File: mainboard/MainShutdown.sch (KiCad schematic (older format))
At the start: 28 parts, among them K2 G6DN 12V, Q2 DMN10H220L, Q8 NTR5105PT1G, Q9 NTR5105PT1G, SW2 SD_RESET, U13 TS3704IPT, U14 CD4044, U15 CD4082, U4 MainBoard_AD8244

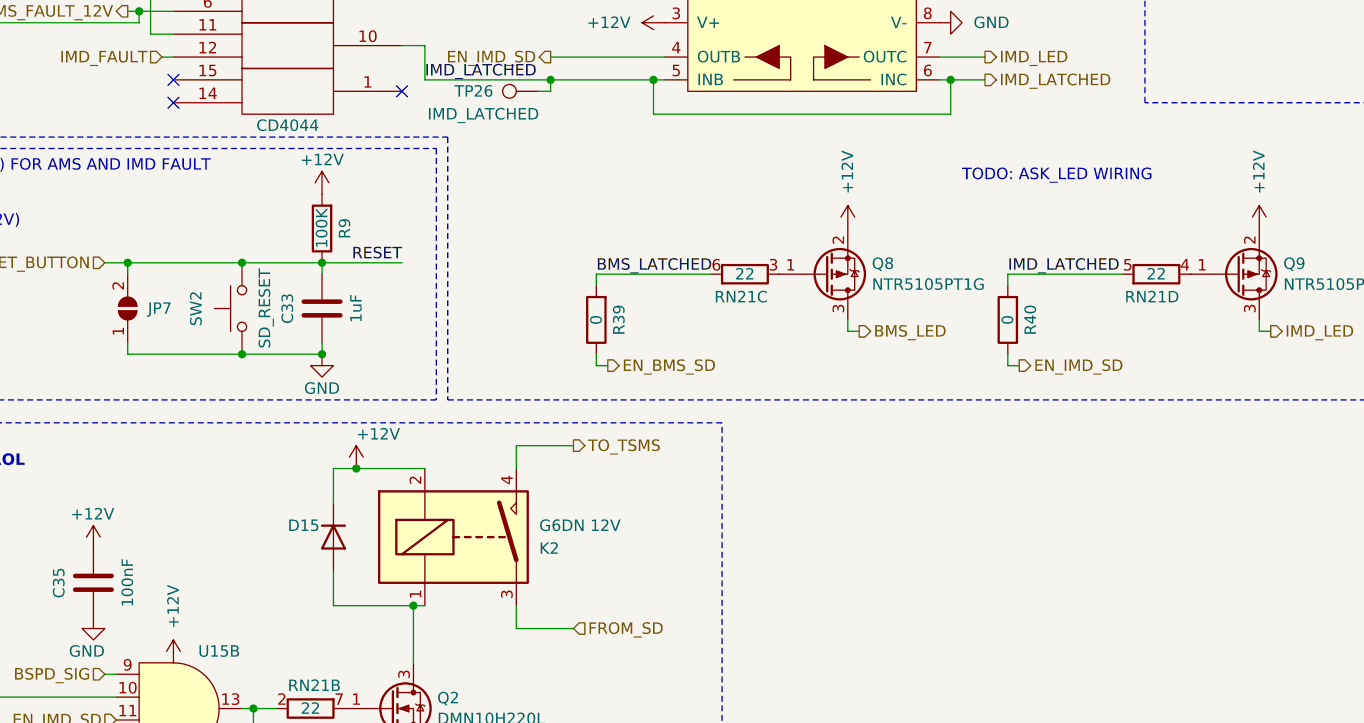
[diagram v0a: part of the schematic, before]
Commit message: Renamed handcart detection
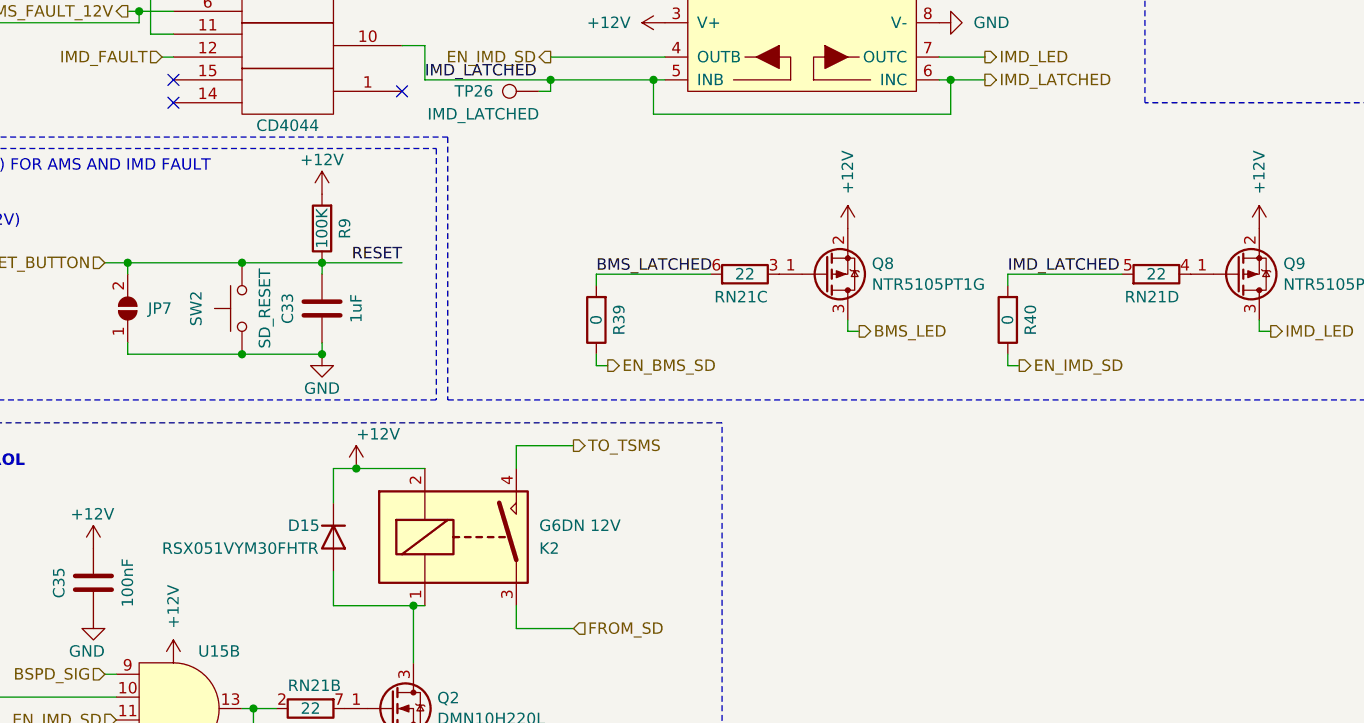
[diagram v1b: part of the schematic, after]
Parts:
- D15: value D -> RSX051VYM30FHTR
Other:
- note removed: "TODO: ASK_LED WIRING\n"
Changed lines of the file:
@@
 AR Path="/5B045B0D/5E3C4855" Ref="D15"  Part="1"
 F 0 "D15" V 3250 3950 50  0000 L CNN
-F 1 "D" V 3350 3950 50  0001 L CNN
+F 1 "RSX051VYM30FHTR" V 3350 3400 50  0000 L CNN
 F 2 "MainBoard:SOD_323HE" H 3300 4150 50  0001 C CNN
 F 3 "~" H 3300 4150 50  0001 C CNN
@@
 	1    0    0    1
 $EndComp
-Text Notes 6050 2600 0    50   ~ 0
-TODO: ASK_LED WIRING\n
 Wire Wire Line
 	9250 5900 9300 5900

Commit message: Correction almost finished, Started layouting
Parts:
- removed C35, C47: 100nF, Capacitor_SMD:C_0603_1608Metric, symbol Device:C
- removed D14: DDZ13ASF 13V, Diode_SMD:D_SOD-323, symbol Device:D_Zener
- removed D15: RSX051VYM30FHTR, MainBoard:SOD_323HE, symbol Device:D
- removed JP7: SolderJumper_2_Open, Jumper:SolderJumper-2_P1.3mm_Open_RoundedPad1.0x1.5mm, symbol Jumper:SolderJumper_2_Open
- removed K2: G6DN 12V, MainBoard:G6DN-1A_DC12, symbol Relay:UMS05-1A80-75L
- removed Q8, Q9: NTR5105PT1G, Package_TO_SOT_SMD:SOT-23, symbol Device:Q_PMOS_GSD
- removed R39, R40: 0, Resistor_SMD:R_0603_1608Metric, symbol Device:R
- removed R54: 1M, Resistor_SMD:R_0603_1608Metric, symbol Device:R
- removed U13: TS3704IPT, Package_SO:TSSOP-14_4.4x5mm_P0.65mm, symbol MainBoard:TS3704
- removed U15: CD4082, Package_SO:TSSOP-14_4.4x5mm_P0.65mm, symbol MainBoard:CD4082
- removed U4: MainBoard_AD8244, Package_SO:MSOP-10_3x3mm_P0.5mm, symbol MainBoard:MainBoard_AD8244
- added D15: 1N4148W, Diode_SMD:D_SOD-123, symbol Diode:1N4148W
- added K2: OJE-SH-112DM, Eagle_Main:OJE-SH-112DM, symbol Eagle_Main:OJE-SH-112DM
- added Q13, Q14, Q15: DMN10H220L, Package_TO_SOT_SMD:SOT-23, symbol Transistor_FET:DMN10H220L
- added R38: 100K, Resistor_SMD:R_0603_1608Metric, symbol Device:R
- added RN23: 22, Resistor_SMD:R_Array_Convex_4x0603, symbol Device:R_Pack04_Split
- added RN24: 330k, Resistor_SMD:R_Array_Convex_4x0603, symbol Device:R_Pack04
- added TP32: EXT_LATCHED, TestPoint:TestPoint_Pad_D1.0mm, symbol Connector:TestPoint
- added U17: TS3704, Package_SO:TSSOP-14_4.4x5mm_P0.65mm, symbol Eagle_Main:TS3704
- RN13, RN21: footprint MainBoard:R_network_4x1_bourns_CAY16 -> Resistor_SMD:R_Array_Convex_4x0603
- SW2: footprint MainBoard:Button_SMD_6x3.5x4.3mm -> Button_Switch_SMD:SW_SPST_FSMSM; symbol MainBoard:SW_Push -> Switch:SW_Push
- TP24: value SD_OK -> SD_RELAY_D
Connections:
- net BMS_FAULT_12V is gone; now on net BMS_FAULT: U14.6
- net RESET_BUTTON is gone; now on net SD_RESET: C33.1, R9.1, SW2.1, U14.11, U14.7
- net SD_STATUS is gone; now on net VREF_1.5V: RN13.8 (R1.2)
- net TS_ON_12V is gone; now on net TS_ON: TP28.1
- net +12V: now also D15.1 (K), K2.2, U17.3 (V+); no longer RN13.1 (R1.1)
- net +3V3: now also RN13.1 (R1.1), U17.10 (-), U17.8 (-); no longer RN13.2 (R2.1)
- net BMS_FAULT: now also U17.2
- net BMS_LATCHED: now also RN23.4 (R4.1), U17.9 (+); no longer RN21.6 (R3.2)
- net GND: now also RN13.2 (R2.1), Q15.2 (S), R38.1, RN24.1 (R1.1), RN24.2 (R2.1), RN24.3 (R3.1), RN24.4 (R4.1), U17.12 (V-); no longer Q2.2 (S), RN13.3 (R3.1)
- net IMD_LATCHED: now also RN23.3 (R3.1), U17.11 (+); no longer RN21.5 (R4.2)
- net TS_ON: now also RN23.1 (R1.1), U17.1; no longer TP27.1
- net VREF_1.5V: now also U17.4 (-), U17.6 (-); no longer RN13.6 (R3.2)
- net EXT_LATCHED: now reaches U14.13
- net EXT_LATCHED: now also RN23.2 (R2.1), TP32.1
- net SD_RESET: now reaches U14.3
- net SD_RESET: now also R38.2
- net EXT_FAULT: now reaches U14.4
- net SD_RELAY_D: now reaches Q2.3 (D)
- net SD_RELAY_D: now also TP24.1, D15.2 (A), K2.1
- net at Q2.1 (G): now also RN23.8 (R1.2), RN24.5 (R4.2); no longer RN21.7 (R2.2)
- net IMD_COCKPIT: now reaches RN21.4 (R4.1)
- net BMS_COCKPIT: now reaches RN21.3 (R3.1)
- net SD_OK: no longer names the net of RN21.2 (R2.1)
- net SD_OK: no longer TP24.1
- new net: Q13.3 (D), Q2.2 (S)
- new net: RN21.5 (R4.2), U17.13
- new net: RN21.6 (R3.2), U17.14
- new net: Q13.1 (G), RN23.7 (R2.2), RN24.6 (R3.2)
- new net: Q13.2 (S), Q14.3 (D)
- new net: Q14.1 (G), RN23.6 (R3.2), RN24.7 (R2.2)
- new net: Q14.2 (S), Q15.3 (D)
- new net: Q15.1 (G), RN23.5 (R4.2), RN24.8 (R1.2)
- new net BMS_FAULT_3V3: U17.5 (+)
- new net SD_IN: K2.3
- new net SD_OUT: K2.4
- new net TS_ON_3V3: TP27.1, U17.7 (+)
- no-connect marks 10 -> 9
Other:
- note added: "COCKPIT LEDs"
- note added: "SHUTDOWN CONTROL"
- note added: "normally:\nRESET HIGH\n_FAULT HIGH > _LATCHED HIGH\nfault:\n_FAULT FALLING > _LATCHED LOW (holding)\nresetting:\n_FAULT HIGH\nRESET FALLING > _LATCHED HIGH"
- note removed: "Buffering signals, CD4044 can't \nsource/sink more than 1mA.\nCan be not placed if jumpers are in place"
- note removed: "NORMALLY:\nRESET HIGH\n_FAULT HIGH > _LATCHED HIGH\nFAULT:\n_FAULT FALLING > _LATHCED LOW (holding)\nRESETTING:\n_FAULT HIGH\nRESET FALLING > _LATHCED HIGH"
- note removed: "SHUTDOWN STATUS"
- note removed: "TRACTIVE SYSTEM CONTROL"
- note removed: "Vin=12V\nR=10K-->14.4mW\nVref_1V5\nR=100K-->0.06mW"
- moved on the sheet: C32, C33, C34, Q2, R9, RN13, RN21B, RN21C, RN21D, SW2, TP24, TP25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
